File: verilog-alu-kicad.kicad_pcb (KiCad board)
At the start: 2 copper layers, 9 parts

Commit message: try wiring
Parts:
- removed VCC&GND1, decoder_2&decoder_4: Conn_01x02_MountingPin, Connector_PinHeader_2.54mm:PinHeader_1x03_P2.54mm_Horizontal
- added A&B: Conn_01x02, Connector_PinHeader_2.54mm:PinHeader_1x02_P2.54mm_Vertical, F.Cu at (57.1, -685.8)
- added VCC&GND: Conn_01x02, Connector_PinHeader_2.54mm:PinHeader_1x02_P2.54mm_Vertical, F.Cu at (57.1, -673.1)
- C&decoder_0, Cout&Sout1, InputSelector&OutputSelector1: value Conn_01x02_MountingPin -> Conn_01x02; footprint Connector_PinHeader_2.54mm:PinHeader_1x03_P2.54mm_Horizontal -> Connector_PinHeader_2.54mm:PinHeader_1x02_P2.54mm_Vertical
- moved InputSelector&OutputSelector1 52.3 mm to (96.5, -694.7)
- moved C&decoder_0 47.7 mm to (77.5, -694.7)
- moved NAND-IC-3 44.3 mm to (77.5, -685.8)
- moved NAND-IC-1 36.7 mm to (62.2, -685.8)
- moved NAND-IC-4 27.5 mm to (108.0, -685.8)
- moved NAND-IC-2 21.3 mm to (92.7, -685.8)
- moved Cout&Sout1 14.4 mm to (101.6, -662.9)
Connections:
- NAND-IC-3 pad 1: Net-(C&decoder_0-Pad2) -> Net-(C&decoder_0-Pad1)
- NAND-IC-3 pad 2: Net-(C&decoder_0-Pad1) -> Net-(C&decoder_0-Pad2)
- NAND-IC-3 pad 5: Net-(InputSelector&OutputSelector1-Pad2) -> Net-(InputSelector&OutputSelector1-Pad1)
- NAND-IC-4 pad 1: Net-(InputSelector&OutputSelector1-Pad1) -> Net-(InputSelector&OutputSelector1-Pad2)
- NAND-IC-4 pad 2: Net-(InputSelector&OutputSelector1-Pad1) -> Net-(InputSelector&OutputSelector1-Pad2)
- NAND-IC-4 pad 5: Net-(InputSelector&OutputSelector1-Pad1) -> Net-(InputSelector&OutputSelector1-Pad2)
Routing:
- net Net-(JVCC&GND1-Pad1): track 0.00 -> 76.2 mm
- net Net-(JVCC&GND1-Pad2): track 0.00 -> 52.9 mm
- net Net-(NAND-IC-1-Pad3): track 0.00 -> 30.9 mm
- net Net-(NAND-IC-1-Pad11): track 0.00 -> 23.8 mm
- net Net-(A&B1-Pad2): track 0.00 -> 15.9 mm
- net Net-(NAND-IC-1-Pad13): track 0.00 -> 14.8 mm
- net Net-(A&B1-Pad1): track 0.00 -> 13.6 mm
- net Net-(C&decoder_0-Pad1): track 0.00 -> 11.0 mm
- net Net-(NAND-IC-1-Pad12): track 0.00 -> 10.8 mm
- net Net-(C&decoder_0-Pad2): track 0.00 -> 9.94 mm
- net Net-(NAND-IC-3-Pad3): track 0.00 -> 2.54 mm

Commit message: 完成したんじゃね？
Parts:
- moved Cout&Sout1 34.1 mm to (85.2, -692.9)
- moved InputSelector&OutputSelector1 6.90 mm to (89.9, -692.9)
- moved C&decoder_0 3.59 mm to (80.6, -692.9)
- renumbered A&B to A&B1, VCC&GND to JVCC&GND1
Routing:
- net Net-(Cout&Sout1-Pad1): track 0.00 -> 58.2 mm
- net Net-(Cout&Sout1-Pad2): track 0.00 -> 42.8 mm
- net Net-(InputSelector&OutputSelector1-Pad2): track 0.00 -> 31.2 mm
- net Net-(NAND-IC-2-Pad10): track 0.00 -> 30.2 mm
- net Net-(InputSelector&OutputSelector1-Pad1): track 0.00 -> 29.1 mm
- net Net-(NAND-IC-2-Pad3): track 0.00 -> 22.3 mm
- net Net-(NAND-IC-2-Pad11): track 0.00 -> 18.2 mm
- net Net-(NAND-IC-2-Pad13): track 0.00 -> 14.9 mm
- net Net-(NAND-IC-2-Pad12): track 0.00 -> 10.8 mm
- net Net-(NAND-IC-4-Pad12): track 0.00 -> 10.8 mm
- net Net-(NAND-IC-4-Pad10): track 0.00 -> 9.72 mm
- net Net-(NAND-IC-1-Pad11): track 23.8 -> 32.9 mm
- net Net-(JVCC&GND1-Pad2): track 52.9 -> 54.4 mm
- net Net-(C&decoder_0-Pad1): track 11.0 -> 9.74 mm
- net Net-(JVCC&GND1-Pad1): track 76.2 -> 75.2 mm
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
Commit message: update for print
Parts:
- added REF**: MountingHole_3.5mm, kicad-hole:MountingHole_3.5mm, F.Cu at (121.9, -662.9)
- added REF**: MountingHole_3.5mm, kicad-hole:MountingHole_3.5mm, F.Cu at (52.1, -693.4)
- added REF**: MountingHole_3.5mm, kicad-hole:MountingHole_3.5mm, F.Cu at (52.1, -662.9)
- added REF**: MountingHole_3.5mm, kicad-hole:MountingHole_3.5mm, F.Cu at (121.9, -693.4)
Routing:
- net Net-(NAND-IC-4-Pad13): track 0.00 -> 13.6 mm
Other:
- board text added: "1bit Arithmetic Logic Unit by NITKC 4J 2019 Verilog Source: https://github.com/NITKC-16s/alu-verilog Hardware Source: https://github.com/NITKC-16s/alu-kicad"
- board text added: "A"
- board text added: "B"
- board text added: "C"
- board text added: "Cout"
- board text added: "GND"
- board text added: "InputSelect"
- board text added: "OutputSelect"
- board text added: "Sout"
- board text added: "VCC"
- board text added: "decoder[0]"

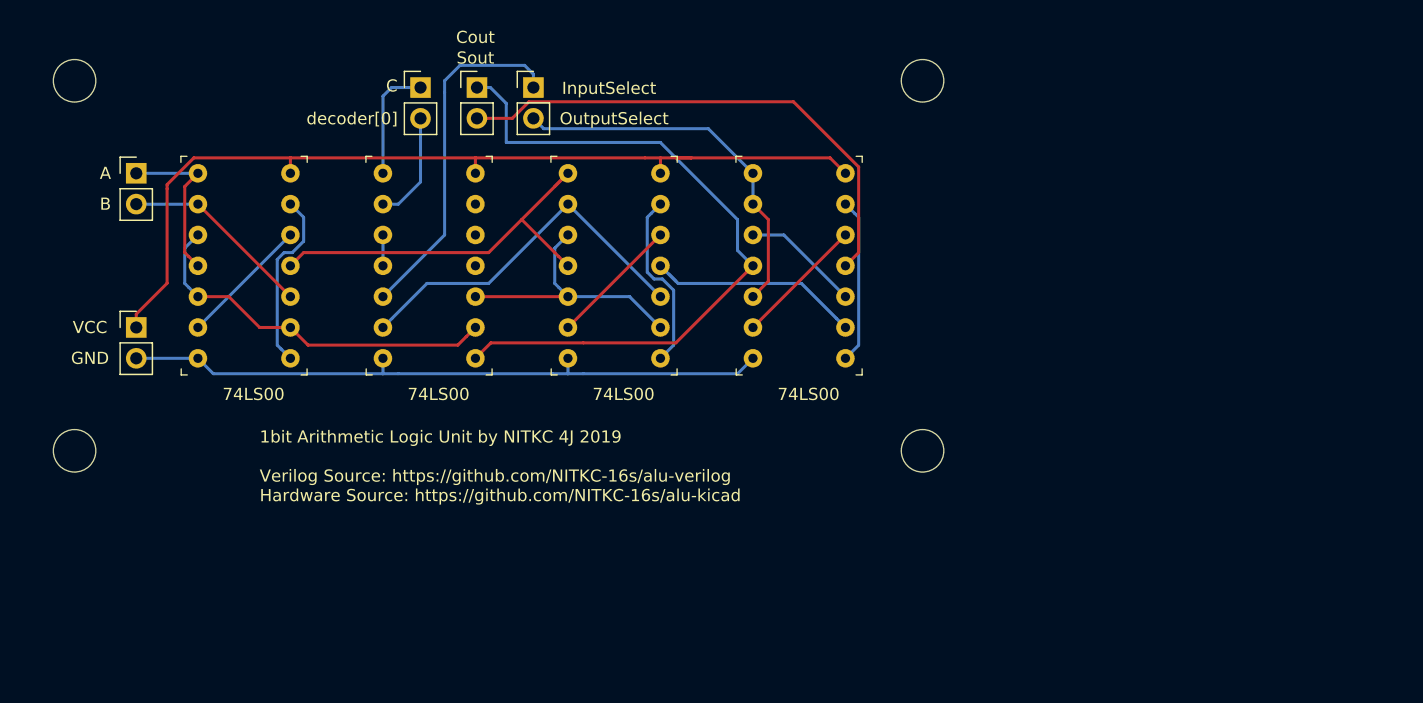
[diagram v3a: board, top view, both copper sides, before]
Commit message: set origin and frame line
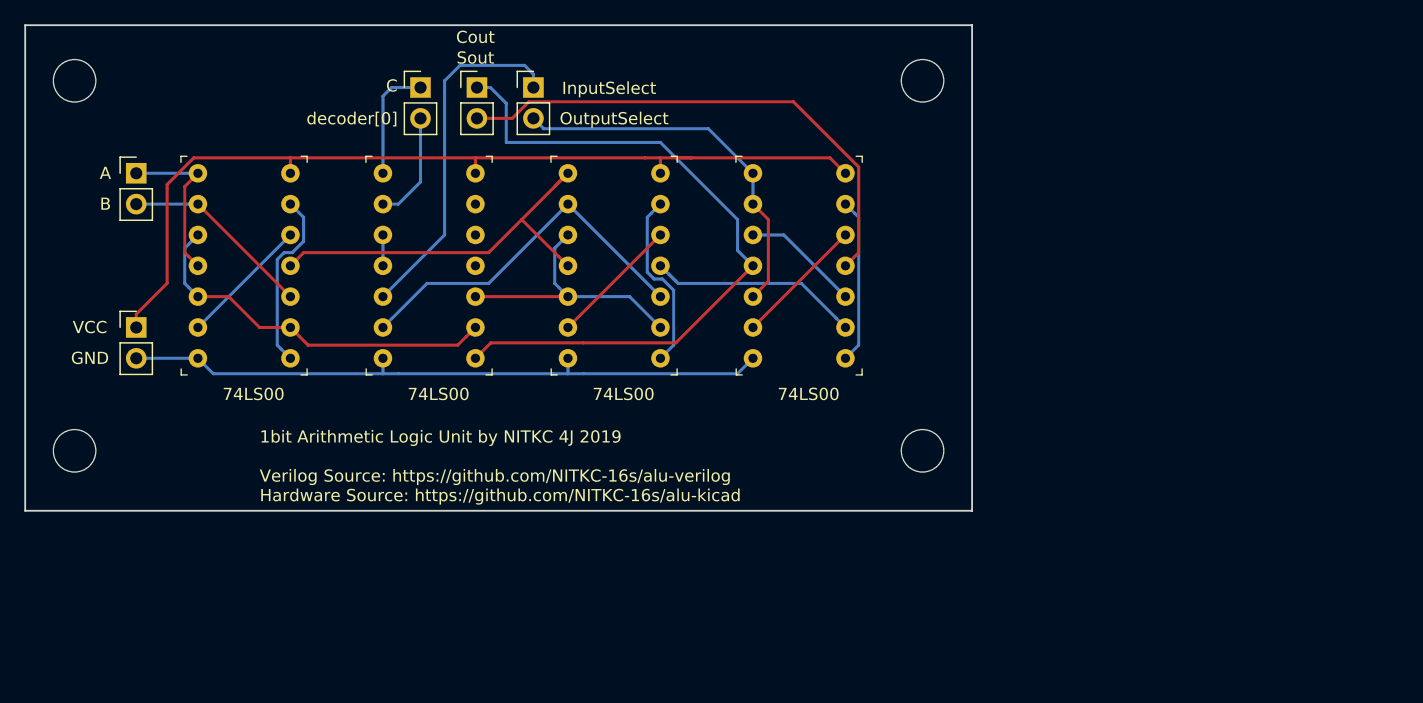
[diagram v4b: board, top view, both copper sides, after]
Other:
- board outline added: 78 x 40 mm
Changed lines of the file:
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@@
     (pad_to_mask_clearance 0.051)
     (solder_mask_min_width 0.25)
-    (aux_axis_origin 0 0)
+    (aux_axis_origin 48 -658)
     (visible_elements FFFFFF7F)
     (pcbplotparams
@@
     )
   )
-  (gr_line (start 126 -658) (end 126 -698) (layer Eco2.User) (width 0.15))
-  (gr_line (start 48 -658) (end 126 -658) (layer Eco2.User) (width 0.15))
+  (gr_line (start 126 -658) (end 126 -698) (layer Edge.Cuts) (width 0.15))
+  (gr_line (start 48 -658) (end 126 -658) (layer Edge.Cuts) (width 0.15))
   (dimension 78 (width 0.15) (layer Eco2.User)
     (gr_text "78.000 mm" (at 87 -701.3) (layer Eco2.User)
@@
     (arrow2b (pts (xy 46.000001 -698) (xy 46.586422 -696.873496)))
   )
-  (gr_line (start 48 -698) (end 48 -658) (layer Eco2.User) (width 0.15))
-  (gr_line (start 126 -698) (end 48 -698) (layer Eco2.User) (width 0.15))
+  (gr_line (start 48 -698) (end 48 -658) (layer Edge.Cuts) (width 0.15))
+  (gr_line (start 126 -698) (end 48 -698) (layer Edge.Cuts) (width 0.15))
   (gr_text GND (at 53.34 -670.56) (layer F.SilkS)
     (effects (font (size 1 1) (thickness 0.15)))
